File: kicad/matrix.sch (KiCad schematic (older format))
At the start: 152 parts

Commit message: Switched to 0603 and redrawn the PCB
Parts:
- D1, D10, D11, D12, D13, D14, D15, D16, D17, D18, D19, D2, D20, D21, D22, D23, D24, D25, D26, D27, D28, D29, D3, D30, D31, D32, D33, D34, D35, D36, D37, D38, D39, D4, D40, D41, D42, D43, D44, D45, D46, D47, D48, D49, D5, D50, D51, D52, D53, D54, D55, D56, D57, D58, D59, D6, D60, D61, D62, D63, D64, D65, D66, D67, D68, D69, D7, D70, D71, D72, D73, D74, D75, D76, D8, D9: footprint Diode_SMD:D_1206_3216Metric_Pad1.42x1.75mm_HandSolder -> Diode_SMD:D_0603_1608Metric_Pad1.05x0.95mm_HandSolder

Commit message: Changed diode footprint to the more used sod-123
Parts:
- D1, D10, D11, D12, D13, D14, D15, D16, D17, D18, D19, D2, D20, D21, D22, D23, D24, D25, D26, D27, D28, D29, D3, D30, D31, D32, D33, D34, D35, D36, D37, D38, D39, D4, D40, D41, D42, D43, D44, D45, D46, D47, D48, D49, D5, D50, D51, D52, D53, D54, D55, D56, D57, D58, D59, D6, D60, D61, D62, D63, D64, D65, D66, D67, D68, D69, D7, D70, D71, D72, D73, D74, D75, D76, D8, D9: footprint Diode_SMD:D_0603_1608Metric_Pad1.05x0.95mm_HandSolder -> Diode_SMD:D_SOD-123

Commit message: Adding crazy many options for bottom row
this is going to be rev4
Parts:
- added D77, D78: 1N4148W, Diode_SMD:D_SOD-123, symbol Diode:1N4148W
- added MX77, MX78, MX79, MX80, MX81, MX82, MX83, MX84: MX-NoLED, index-tab:Kailh_socket_MX, symbol MX_Alps_Hybrid:MX-NoLED
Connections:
- net COL3: now also MX79.1 (COL)
- net COL4: now also MX80.1 (COL)
- net COL5: now also MX77.1 (COL), MX81.1 (COL)
- net COL6: now also MX82.1 (COL)
- net COL7: now also MX78.1 (COL), MX83.1 (COL)
- net COL8: now also MX84.1 (COL)
- net ROW5: now also D77.1 (K), D78.1 (K)
- net at D24.2 (A), MX24.2 (ROW): now also MX79.2 (ROW)
- net at D30.2 (A), MX30.2 (ROW): now also MX80.2 (ROW)
- net at D41.2 (A), MX41.2 (ROW): now also MX82.2 (ROW)
- net at D52.2 (A), MX52.2 (ROW): now also MX84.2 (ROW)
- new net: D77.2 (A), MX77.2 (ROW), MX81.2 (ROW)
- new net: D78.2 (A), MX78.2 (ROW), MX83.2 (ROW)
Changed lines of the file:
@@
 Connection ~ 7500 3550
 Wire Wire Line
-	4200 5850 5200 5850
-Wire Wire Line
-	3200 5850 4200 5850
+	4200 5850 4700 5850
 Wire Wire Line
 	2000 700  2000 1000
@@
 Wire Wire Line
 	1500 1000 1500 1850
+$Comp
+L MX_Alps_Hybrid:MX-NoLED MX?
+U 1 1 5ECDD491
+P 3850 5300
+AR Path="/5ECDD491" Ref="MX?"  Part="1"
+AR Path="/5E539A90/5ECDD491" Ref="MX77"  Part="1"
+F 0 "MX77" H 3932 5524 60  0000 C CNN
+F 1 "MX-NoLED" H 3932 5450 20  0000 C CNN
+F 2 "index-tab:Kailh_socket_MX" H 3225 5275 60  0001 C CNN
+F 3 "" H 3225 5275 60  0001 C CNN
+	1    3850 5300
+	1    0    0    -1
+$EndComp
+Wire Wire Line
+	4000 4400 4000 5250
+$Comp
+L MX_Alps_Hybrid:MX-NoLED MX?
+U 1 1 5ECF60EA
+P 4850 5300
+AR Path="/5ECF60EA" Ref="MX?"  Part="1"
+AR Path="/5E539A90/5ECF60EA" Ref="MX78"  Part="1"
+F 0 "MX78" H 4932 5524 60  0000 C CNN
+F 1 "MX-NoLED" H 4932 5450 20  0000 C CNN
+F 2 "index-tab:Kailh_socket_MX" H 4225 5275 60  0001 C CNN
+F 3 "" H 4225 5275 60  0001 C CNN
+	1    4850 5300
+	1    0    0    -1
+$EndComp
+Wire Wire Line
+	5000 4400 5000 5250
+Wire Wire Line
+	3200 5850 3700 5850
+$Comp
+L Diode:1N4148W D77
+U 1 1 5ED2AB81
+P 3700 5700
+F 0 "D77" V 3746 5620 50  0000 R CNN
+F 1 "1N4148W" V 3655 5620 50  0000 R CNN
+F 2 "Diode_SMD:D_SOD-123" H 3700 5525 50  0001 C CNN
+F 3 "https://www.vishay.com/docs/85748/1n4148w.pdf" H 3700 5700 50  0001 C CNN
+	1    3700 5700
+	0    -1   -1   0
+$EndComp
+$Comp
+L Diode:1N4148W D78
+U 1 1 5ED4386F
+P 4700 5700
+F 0 "D78" V 4746 5620 50  0000 R CNN
+F 1 "1N4148W" V 4655 5620 50  0000 R CNN
+F 2 "Diode_SMD:D_SOD-123" H 4700 5525 50  0001 C CNN
+F 3 "https://www.vishay.com/docs/85748/1n4148w.pdf" H 4700 5700 50  0001 C CNN
+	1    4700 5700
+	0    -1   -1   0
+$EndComp
+Connection ~ 3700 5850
+Wire Wire Line
+	3700 5850 4200 5850
+Connection ~ 4700 5850
+Wire Wire Line
+	4700 5850 5200 5850
+Wire Wire Line
+	3700 5550 3700 5450
+Wire Wire Line
+	3700 5450 3800 5450
+Wire Wire Line
+	4700 5550 4700 5450
+Wire Wire Line
+	4700 5450 4800 5450
+$Comp
+L MX_Alps_Hybrid:MX-NoLED MX?
+U 1 1 5EDC9716
+P 2950 6150
+AR Path="/5EDC9716" Ref="MX?"  Part="1"
+AR Path="/5E539A90/5EDC9716" Ref="MX79"  Part="1"
+F 0 "MX79" H 3032 6374 60  0000 C CNN
+F 1 "MX-NoLED" H 3032 6300 20  0000 C CNN
+F 2 "index-tab:Kailh_socket_MX" H 2325 6125 60  0001 C CNN
+F 3 "" H 2325 6125 60  0001 C CNN
+	1    2950 6150
+	1    0    0    -1
+$EndComp
+Wire Wire Line
+	2800 5450 2800 6300
+Wire Wire Line
+	2800 6300 2900 6300
+Connection ~ 2800 5450
+$Comp
+L MX_Alps_Hybrid:MX-NoLED MX?
+U 1 1 5EE09920
+P 3450 6150
+AR Path="/5EE09920" Ref="MX?"  Part="1"
+AR Path="/5E539A90/5EE09920" Ref="MX80"  Part="1"
+F 0 "MX80" H 3532 6374 60  0000 C CNN
+F 1 "MX-NoLED" H 3532 6300 20  0000 C CNN
+F 2 "index-tab:Kailh_socket_MX" H 2825 6125 60  0001 C CNN
+F 3 "" H 2825 6125 60  0001 C CNN
+	1    3450 6150
+	1    0    0    -1
+$EndComp
+$Comp
+L MX_Alps_Hybrid:MX-NoLED MX?
+U 1 1 5EE0A330
+P 3950 6150
+AR Path="/5EE0A330" Ref="MX?"  Part="1"
+AR Path="/5E539A90/5EE0A330" Ref="MX81"  Part="1"
+F 0 "MX81" H 4032 6374 60  0000 C CNN
+F 1 "MX-NoLED" H 4032 6300 20  0000 C CNN
+F 2 "index-tab:Kailh_socket_MX" H 3325 6125 60  0001 C CNN
+F 3 "" H 3325 6125 60  0001 C CNN
+	1    3950 6150
+	1    0    0    -1
+$EndComp
+Wire Wire Line
+	3100 6100 3100 5250
+Wire Wire Line
+	3100 5250 3000 5250
+Connection ~ 3000 5250
+Wire Wire Line
+	3300 5450 3300 6300
+Wire Wire Line
+	3300 6300 3400 6300
+Connection ~ 3300 5450
+Wire Wire Line
+	3800 5450 3800 6300
+Wire Wire Line
+	3800 6300 3900 6300
+Connection ~ 3800 5450
+Wire Wire Line
+	3500 5250 3600 5250
+Wire Wire Line
+	3600 5250 3600 6100
+Connection ~ 3500 5250
+Wire Wire Line
+	4000 5250 4100 5250
+Wire Wire Line
+	4100 5250 4100 6100
+Connection ~ 4000 5250
+$Comp
+L MX_Alps_Hybrid:MX-NoLED MX?
+U 1 1 5EE973CF
+P 4450 6150
+AR Path="/5EE973CF" Ref="MX?"  Part="1"
+AR Path="/5E539A90/5EE973CF" Ref="MX82"  Part="1"
+F 0 "MX82" H 4532 6374 60  0000 C CNN
+F 1 "MX-NoLED" H 4532 6300 20  0000 C CNN
+F 2 "index-tab:Kailh_socket_MX" H 3825 6125 60  0001 C CNN
+F 3 "" H 3825 6125 60  0001 C CNN
+	1    4450 6150
+	1    0    0    -1
+$EndComp
+Wire Wire Line
+	4400 6300 4300 6300
+Wire Wire Line
+	4300 6300 4300 5450
+Connection ~ 4300 5450
+Wire Wire Line
+	4500 5250 4600 5250
+Wire Wire Line
+	4600 5250 4600 6100
+Connection ~ 4500 5250
+$Comp
+L MX_Alps_Hybrid:MX-NoLED MX?
+U 1 1 5EED3CF4
+P 4950 6150
+AR Path="/5EED3CF4" Ref="MX?"  Part="1"
+AR Path="/5E539A90/5EED3CF4" Ref="MX83"  Part="1"
+F 0 "MX83" H 5032 6374 60  0000 C CNN
+F 1 "MX-NoLED" H 5032 6300 20  0000 C CNN
+F 2 "index-tab:Kailh_socket_MX" H 4325 6125 60  0001 C CNN
+F 3 "" H 4325 6125 60  0001 C CNN
+	1    4950 6150
+	1    0    0    -1
+$EndComp
+$Comp
+L MX_Alps_Hybrid:MX-NoLED MX?
+U 1 1 5EED4245
+P 5450 6150
+AR Path="/5EED4245" Ref="MX?"  Part="1"
+AR Path="/5E539A90/5EED4245" Ref="MX84"  Part="1"
+F 0 "MX84" H 5532 6374 60  0000 C CNN
+F 1 "MX-NoLED" H 5532 6300 20  0000 C CNN
+F 2 "index-tab:Kailh_socket_MX" H 4825 6125 60  0001 C CNN
+F 3 "" H 4825 6125 60  0001 C CNN
+	1    5450 6150
+	1    0    0    -1
+$EndComp
+Wire Wire Line
+	5400 6300 5300 6300
+Wire Wire Line
+	5300 6300 5300 5450
+Connection ~ 5300 5450
+Wire Wire Line
+	4900 6300 4800 6300
+Wire Wire Line
+	4800 6300 4800 5450
+Connection ~ 4800 5450
+Wire Wire Line
+	5100 6100 5100 5250
+Wire Wire Line
+	5100 5250 5000 5250
+Connection ~ 5000 5250
+Wire Wire Line
+	5600 6100 5600 5250
+Wire Wire Line
+	5600 5250 5500 5250
+Connection ~ 5500 5250
 $EndSCHEMATC

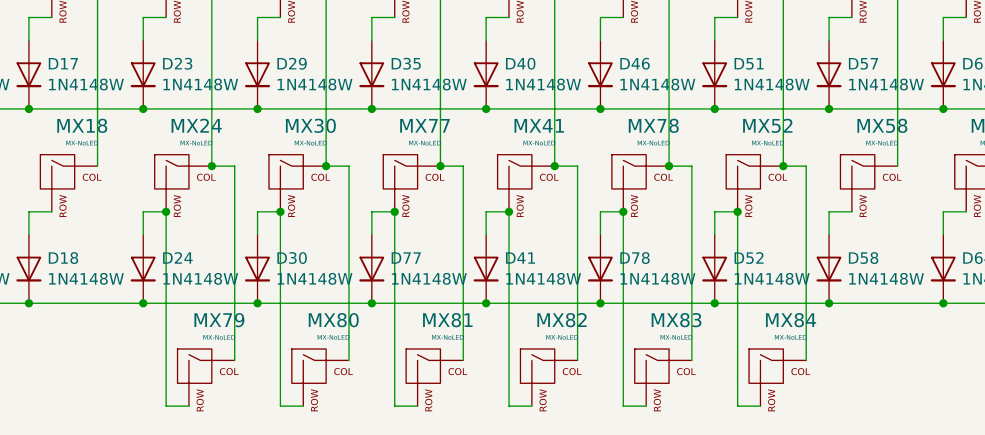
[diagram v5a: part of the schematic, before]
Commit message: rev5: fixed 2x2u and 7u stabs
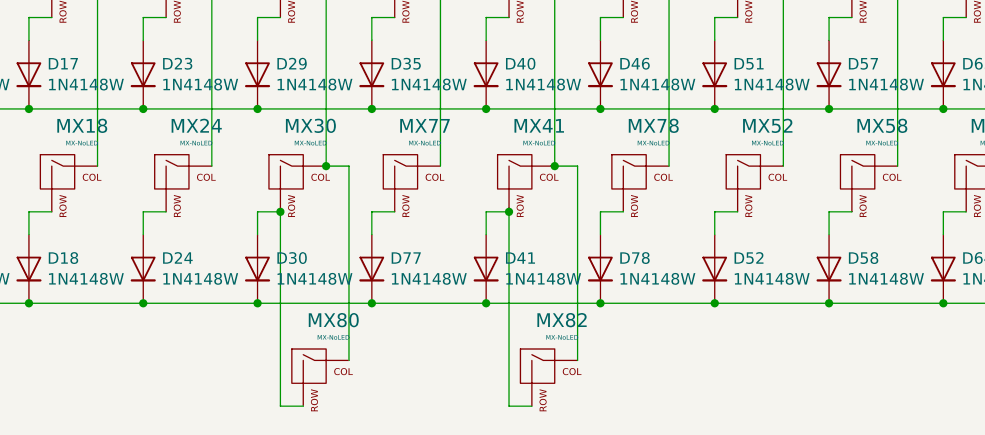
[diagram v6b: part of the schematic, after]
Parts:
- removed MX79, MX81, MX83, MX84: MX-NoLED, index-tab:Kailh_socket_MX, symbol MX_Alps_Hybrid:MX-NoLED
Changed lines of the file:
@@
-$Comp
-L MX_Alps_Hybrid:MX-NoLED MX?
-U 1 1 5EDC9716
-P 2950 6150
-AR Path="/5EDC9716" Ref="MX?"  Part="1"
-AR Path="/5E539A90/5EDC9716" Ref="MX79"  Part="1"
-F 0 "MX79" H 3032 6374 60  0000 C CNN
-F 1 "MX-NoLED" H 3032 6300 20  0000 C CNN
-F 2 "index-tab:Kailh_socket_MX" H 2325 6125 60  0001 C CNN
-F 3 "" H 2325 6125 60  0001 C CNN
-	1    2950 6150
-	1    0    0    -1
-$EndComp
-Wire Wire Line
-	2800 5450 2800 6300
-Wire Wire Line
-	2800 6300 2900 6300
-Connection ~ 2800 5450
 $Comp
 L MX_Alps_Hybrid:MX-NoLED MX?
@@
 	1    0    0    -1
 $EndComp
-$Comp
-L MX_Alps_Hybrid:MX-NoLED MX?
-U 1 1 5EE0A330
-P 3950 6150
-AR Path="/5EE0A330" Ref="MX?"  Part="1"
-AR Path="/5E539A90/5EE0A330" Ref="MX81"  Part="1"
-F 0 "MX81" H 4032 6374 60  0000 C CNN
-F 1 "MX-NoLED" H 4032 6300 20  0000 C CNN
-F 2 "index-tab:Kailh_socket_MX" H 3325 6125 60  0001 C CNN
-F 3 "" H 3325 6125 60  0001 C CNN
-	1    3950 6150
-	1    0    0    -1
-$EndComp
-Wire Wire Line
-	3100 6100 3100 5250
-Wire Wire Line
-	3100 5250 3000 5250
-Connection ~ 3000 5250
 Wire Wire Line
 	3300 5450 3300 6300
@@
 Connection ~ 3300 5450
 Wire Wire Line
-	3800 5450 3800 6300
-Wire Wire Line
-	3800 6300 3900 6300
-Connection ~ 3800 5450
-Wire Wire Line
 	3500 5250 3600 5250
 Wire Wire Line
 	3600 5250 3600 6100
 Connection ~ 3500 5250
-Wire Wire Line
-	4000 5250 4100 5250
-Wire Wire Line
-	4100 5250 4100 6100
-Connection ~ 4000 5250
 $Comp
 L MX_Alps_Hybrid:MX-NoLED MX?
@@
 	4600 5250 4600 6100
 Connection ~ 4500 5250
-$Comp
-L MX_Alps_Hybrid:MX-NoLED MX?
-U 1 1 5EED3CF4
-P 4950 6150
-AR Path="/5EED3CF4" Ref="MX?"  Part="1"
-AR Path="/5E539A90/5EED3CF4" Ref="MX83"  Part="1"
-F 0 "MX83" H 5032 6374 60  0000 C CNN
-F 1 "MX-NoLED" H 5032 6300 20  0000 C CNN
-F 2 "index-tab:Kailh_socket_MX" H 4325 6125 60  0001 C CNN
-F 3 "" H 4325 6125 60  0001 C CNN
-	1    4950 6150
-	1    0    0    -1
-$EndComp
-$Comp
-L MX_Alps_Hybrid:MX-NoLED MX?
-U 1 1 5EED4245
-P 5450 6150
-AR Path="/5EED4245" Ref="MX?"  Part="1"
-AR Path="/5E539A90/5EED4245" Ref="MX84"  Part="1"
-F 0 "MX84" H 5532 6374 60  0000 C CNN
-F 1 "MX-NoLED" H 5532 6300 20  0000 C CNN
-F 2 "index-tab:Kailh_socket_MX" H 4825 6125 60  0001 C CNN
-F 3 "" H 4825 6125 60  0001 C CNN
-	1    5450 6150
-	1    0    0    -1
-$EndComp
-Wire Wire Line
-	5400 6300 5300 6300
-Wire Wire Line
-	5300 6300 5300 5450
-Connection ~ 5300 5450
-Wire Wire Line
-	4900 6300 4800 6300
-Wire Wire Line
-	4800 6300 4800 5450
-Connection ~ 4800 5450
-Wire Wire Line
-	5100 6100 5100 5250
-Wire Wire Line
-	5100 5250 5000 5250
-Connection ~ 5000 5250
-Wire Wire Line
-	5600 6100 5600 5250
-Wire Wire Line
-	5600 5250 5500 5250
-Connection ~ 5500 5250
 Wire Wire Line
 	1500 1850 1500 2700
